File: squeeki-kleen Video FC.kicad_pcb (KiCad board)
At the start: 2 copper layers, 50.8 x 17.8 mm, 56 parts, among them J1 VCC, J2 VOUT, J3 GND, J4 Conn_Coaxial, Q1 MMBT3906

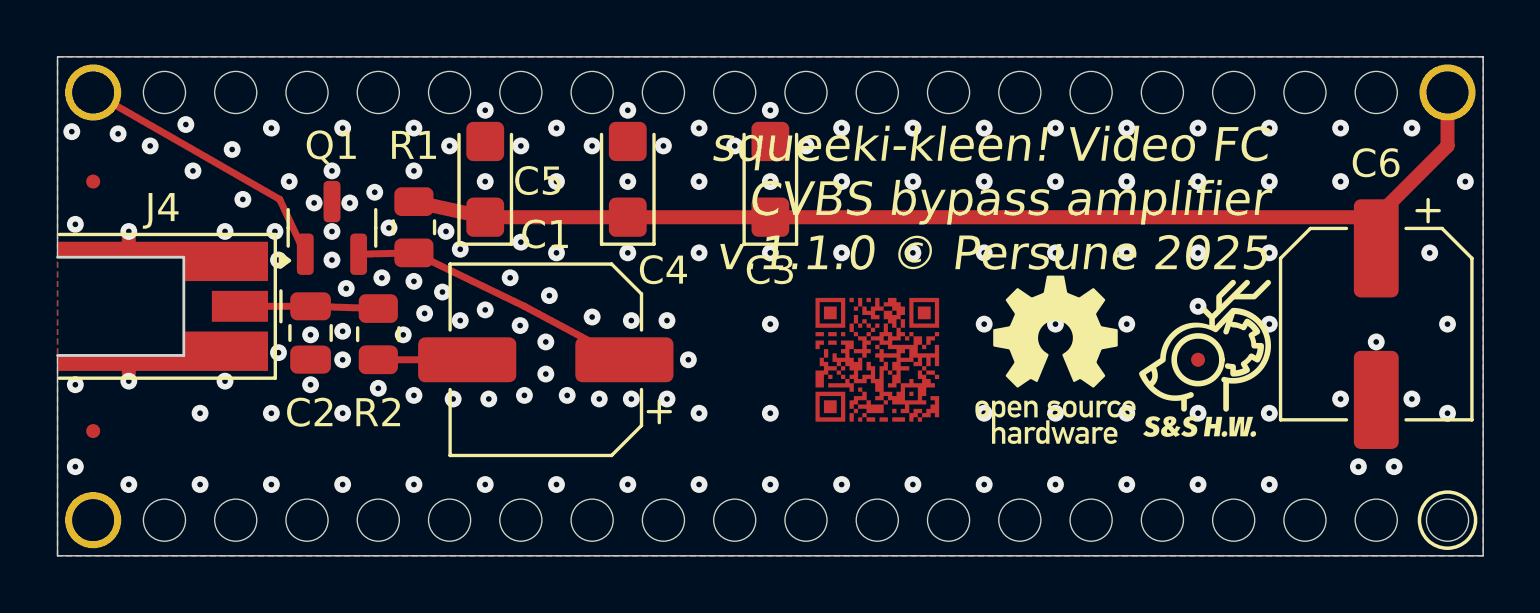
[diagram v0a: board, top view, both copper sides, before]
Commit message: Eevitronics modifications: replace MMCX with solder-wire pads, add fab outputs
See CHANGES.md for the full list of changes (TAPR OHL section 4.2).

Co-Authored-By: Claude Opus 5.5 <noreply@anthropic.com>
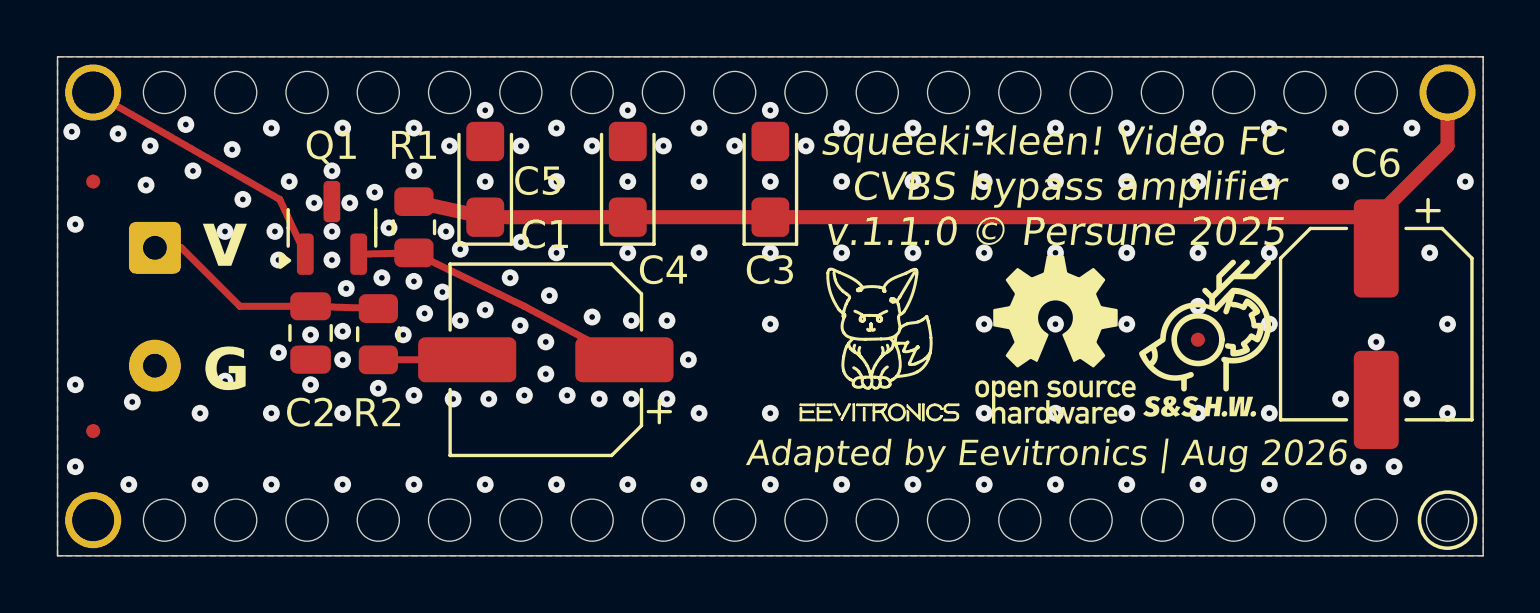
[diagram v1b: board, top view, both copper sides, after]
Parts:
- removed J4: Conn_Coaxial, Connector_Coaxial:MMCX_Molex_73415-0961_Horizontal_0.8mm-PCB
- removed the svg2mod at (67.9, 37.5)
- added GND: Conn_01x02, Connector_Wire:SolderWire-0.25sqmm_1x02_P4.2mm_D0.65mm_OD1.7mm, F.Cu at (42.2, 33.5)
- moved svg2mod 0.72 mm to (79.4, 36.7)
- moved svg2mod 0.72 mm to (74.3, 36.7)
- moved REF** 0.72 mm to (79.4, 36.8)
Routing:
- net /CVBS: track 4.93 -> 8.82 mm
- net GND: track 0.76 -> 0.00 mm
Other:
- outline, holes or cut-outs redrawn
- board text added: "Adapted by Eevitronics | Aug 2026"
- board text added: "G"
- board text added: "V"
- board text removed: "JLCJLCJLCJLC"
